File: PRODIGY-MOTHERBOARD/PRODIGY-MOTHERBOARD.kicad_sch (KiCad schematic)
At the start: 0 parts

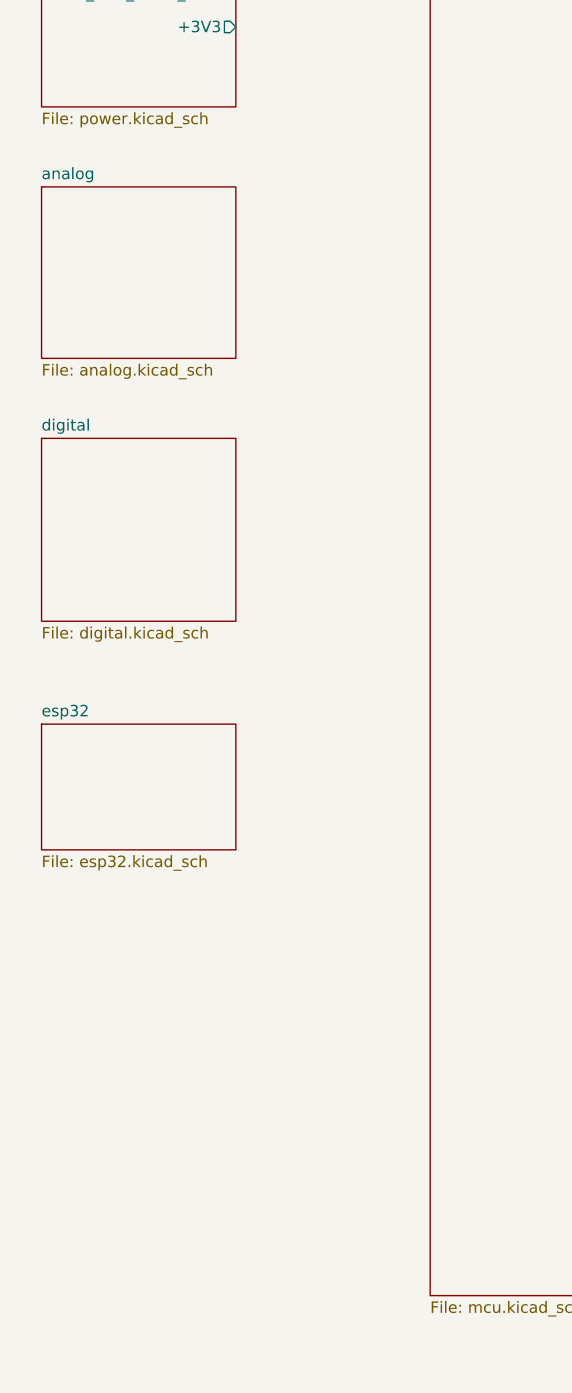
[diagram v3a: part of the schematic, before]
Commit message: Finished neopixel and button's schematic.
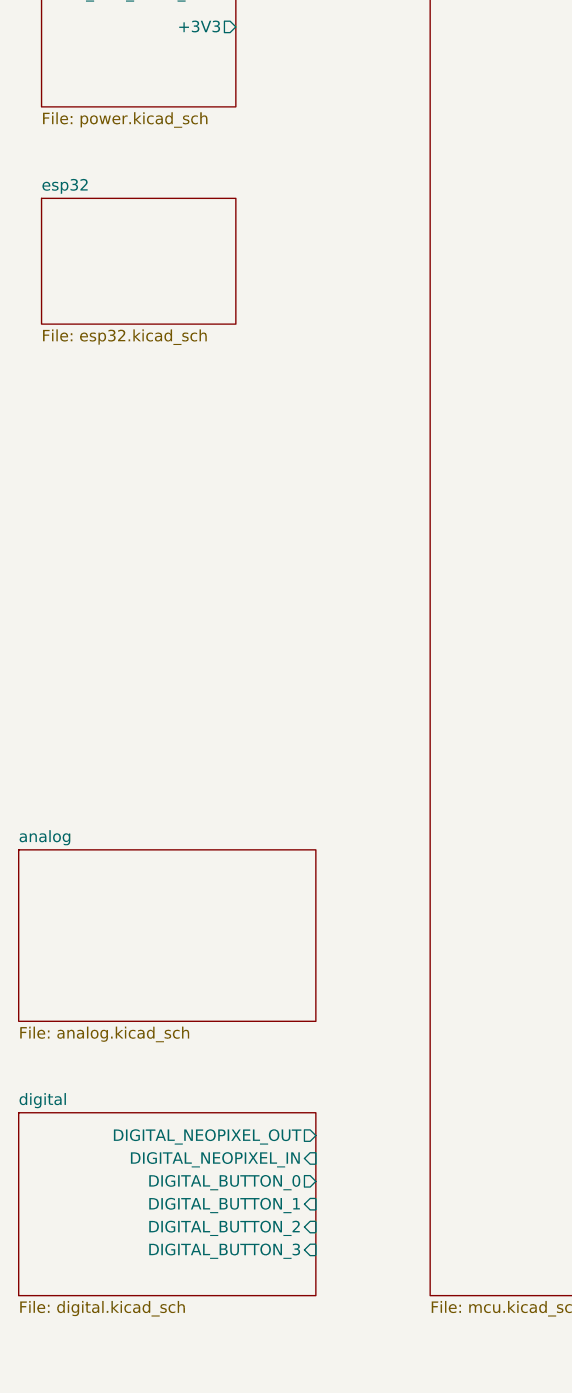
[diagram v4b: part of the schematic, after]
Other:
- sheet digital ports: added DIGITAL_BUTTON_0, DIGITAL_BUTTON_1, DIGITAL_BUTTON_2, DIGITAL_BUTTON_3, DIGITAL_NEOPIXEL_IN, DIGITAL_NEOPIXEL_OUT; removed none
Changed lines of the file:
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@@
 	)
 	(sheet
-		(at 39.37 114.3)
+		(at 39.37 55.88)
 		(size 21.59 13.97)
 		(fields_autoplaced yes)
@@
 		)
 		(property "Sheetname" "esp32"
-			(at 39.37 113.5884 0)
+			(at 39.37 55.1684 0)
 			(effects
 				(font
@@
 		)
 		(property "Sheetfile" "esp32.kicad_sch"
-			(at 39.37 128.8546 0)
+			(at 39.37 70.4346 0)
 			(effects
 				(font
@@
 		)
 		(property "Field2" ""
-			(at 39.37 114.3 0)
+			(at 39.37 55.88 0)
 			(effects
 				(font
@@
 	)
 	(sheet
-		(at 39.37 54.61)
-		(size 21.59 19.05)
+		(at 36.83 128.27)
+		(size 33.02 19.05)
 		(fields_autoplaced yes)
 		(stroke
@@
 		)
 		(property "Sheetname" "analog"
-			(at 39.37 53.8984 0)
+			(at 36.83 127.5584 0)
 			(effects
 				(font
@@
 		)
 		(property "Sheetfile" "analog.kicad_sch"
-			(at 39.37 74.2446 0)
+			(at 36.83 147.9046 0)
 			(effects
 				(font
@@
 		)
 		(property "Field2" ""
-			(at 39.37 54.61 0)
+			(at 36.83 128.27 0)
 			(effects
 				(font
@@
 	)
 	(sheet
-		(at 39.37 82.55)
-		(size 21.59 20.32)
+		(at 36.83 157.48)
+		(size 33.02 20.32)
 		(fields_autoplaced yes)
 		(stroke
@@
 		)
 		(property "Sheetname" "digital"
-			(at 39.37 81.8384 0)
+			(at 36.83 156.7684 0)
 			(effects
 				(font
@@
 		)
 		(property "Sheetfile" "digital.kicad_sch"
-			(at 39.37 103.4546 0)
+			(at 36.83 178.3846 0)
 			(effects
 				(font
@@
 			)
 		)
+		(pin "DIGITAL_NEOPIXEL_IN" input
+			(at 69.85 162.56 0)
+			(effects
+				(font
+					(size 1.27 1.27)
+				)
+				(justify right)
+			)
+		)
+		(pin "DIGITAL_NEOPIXEL_OUT" output
+			(at 69.85 160.02 0)
+			(effects
+				(font
+					(size 1.27 1.27)
+				)
+				(justify right)
+			)
+		)
+		(pin "DIGITAL_BUTTON_1" input
+			(at 69.85 167.64 0)
+			(effects
+				(font
+					(size 1.27 1.27)
+				)
+				(justify right)
+			)
+		)
+		(pin "DIGITAL_BUTTON_2" input
+			(at 69.85 170.18 0)
+			(effects
+				(font
+					(size 1.27 1.27)
+				)
+				(justify right)
+			)
+		)
+		(pin "DIGITAL_BUTTON_3" input
+			(at 69.85 172.72 0)
+			(effects
+				(font
+					(size 1.27 1.27)
+				)
+				(justify right)
+			)
+		)
+		(pin "DIGITAL_BUTTON_0" output
+			(at 69.85 165.1 0)
+			(effects
+				(font
+					(size 1.27 1.27)
+				)
+				(justify right)
+			)
+		)

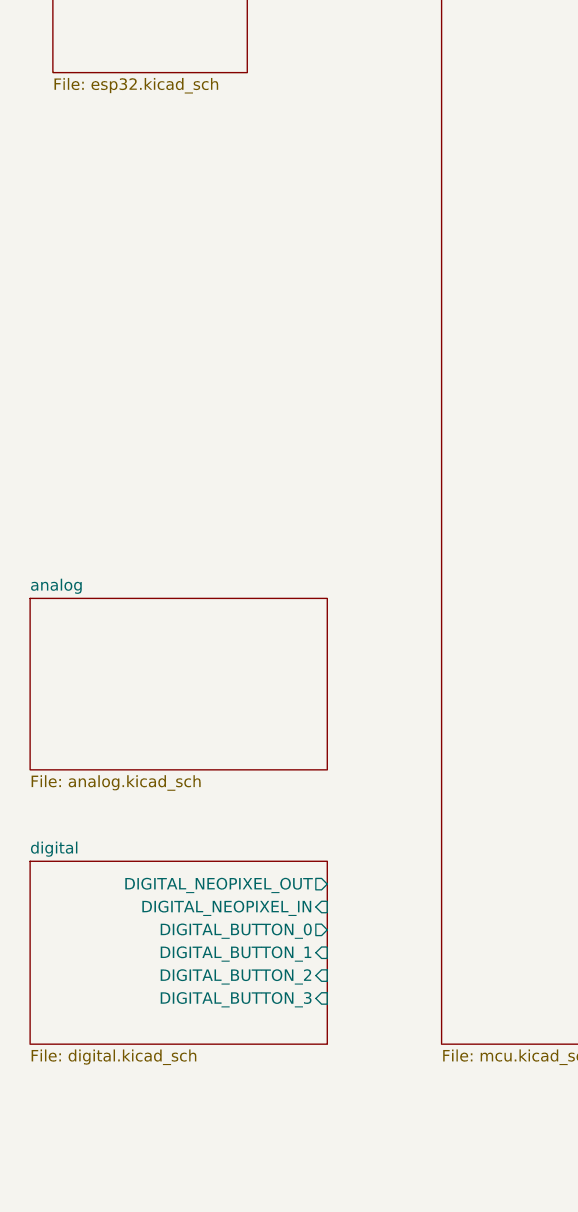
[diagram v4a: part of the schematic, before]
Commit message: LEDs schematic done.
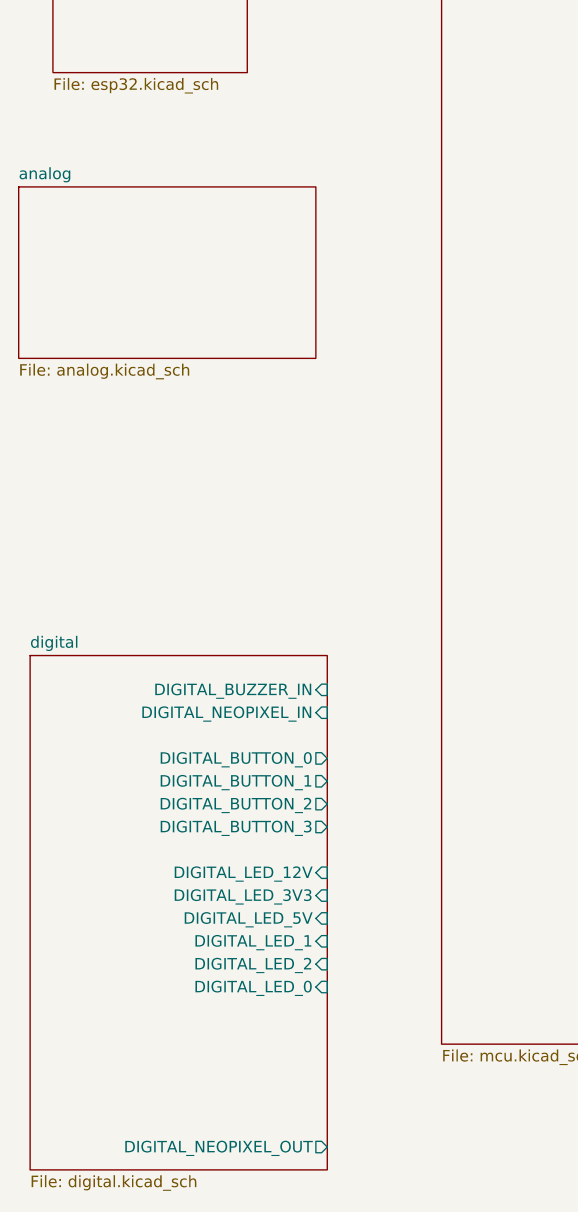
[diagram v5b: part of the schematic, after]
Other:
- sheet digital ports: added DIGITAL_BUZZER_IN, DIGITAL_LED_0, DIGITAL_LED_1, DIGITAL_LED_12V, DIGITAL_LED_2, DIGITAL_LED_3V3, DIGITAL_LED_5V; removed none
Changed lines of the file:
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@@
 	)
 	(sheet
-		(at 36.83 128.27)
+		(at 35.56 82.55)
 		(size 33.02 19.05)
 		(fields_autoplaced yes)
@@
 		)
 		(property "Sheetname" "analog"
-			(at 36.83 127.5584 0)
+			(at 35.56 81.8384 0)
 			(effects
 				(font
@@
 		)
 		(property "Sheetfile" "analog.kicad_sch"
-			(at 36.83 147.9046 0)
+			(at 35.56 102.1846 0)
 			(effects
 				(font
@@
 		)
 		(property "Field2" ""
-			(at 36.83 128.27 0)
+			(at 35.56 82.55 0)
 			(effects
 				(font
@@
 	)
 	(sheet
-		(at 36.83 157.48)
-		(size 33.02 20.32)
+		(at 36.83 134.62)
+		(size 33.02 57.15)
 		(fields_autoplaced yes)
 		(stroke
@@
 		)
 		(property "Sheetname" "digital"
-			(at 36.83 156.7684 0)
+			(at 36.83 133.9084 0)
 			(effects
 				(font
@@
 		)
 		(property "Sheetfile" "digital.kicad_sch"
-			(at 36.83 178.3846 0)
+			(at 36.83 192.3546 0)
 			(effects
 				(font
@@
 		)
 		(pin "DIGITAL_NEOPIXEL_IN" input
-			(at 69.85 162.56 0)
+			(at 69.85 140.97 0)
 			(effects
 				(font
@@
 		)
 		(pin "DIGITAL_NEOPIXEL_OUT" output
-			(at 69.85 160.02 0)
-			(effects
-				(font
-					(size 1.27 1.27)
-				)
-				(justify right)
-			)
-		)
-		(pin "DIGITAL_BUTTON_1" input
-			(at 69.85 167.64 0)
-			(effects
-				(font
-					(size 1.27 1.27)
-				)
-				(justify right)
-			)
-		)
-		(pin "DIGITAL_BUTTON_2" input
-			(at 69.85 170.18 0)
-			(effects
-				(font
-					(size 1.27 1.27)
-				)
-				(justify right)
-			)
-		)
-		(pin "DIGITAL_BUTTON_3" input
-			(at 69.85 172.72 0)
+			(at 69.85 189.23 0)
 			(effects
 				(font
@@
 		)
 		(pin "DIGITAL_BUTTON_0" output
-			(at 69.85 165.1 0)
-			(effects
-				(font
+			(at 69.85 146.05 0)
+			(effects
+				(font
+					(size 1.27 1.27)
+				)
+				(justify right)
+			)
+		)
+		(pin "DIGITAL_BUZZER_IN" input
+			(at 69.85 138.43 0)
+			(effects
+				(font
+					(size 1.27 1.27)
+				)
+				(justify right)
+			)
+		)
+		(pin "DIGITAL_BUTTON_1" output
+			(at 69.85 148.59 0)
+			(effects
+				(font
+					(size 1.27 1.27)
+				)
+				(justify right)
+			)
+		)
+		(pin "DIGITAL_BUTTON_3" output
+			(at 69.85 153.67 0)
+			(effects
+				(font
+					(size 1.27 1.27)
+				)
+				(justify right)
+			)
+		)
+		(pin "DIGITAL_BUTTON_2" output
+			(at 69.85 151.13 0)
+			(effects
+				(font
+					(size 1.27 1.27)
+				)
+				(justify right)
+			)
+		)
+		(pin "DIGITAL_LED_12V" input
+			(at 69.85 158.75 0)
+			(effects
+				(font
+					(size 1.27 1.27)
+				)
+				(justify right)
+			)
+		)
+		(pin "DIGITAL_LED_3V3" input
+			(at 69.85 161.29 0)
+			(effects
+				(font
+					(size 1.27 1.27)
+				)
+				(justify right)
+			)
+		)
+		(pin "DIGITAL_LED_5V" input
+			(at 69.85 163.83 0)
+			(effects
+				(font
+					(size 1.27 1.27)
+				)
+				(justify right)
+			)
+		)
+		(pin "DIGITAL_LED_1" input
+			(at 69.85 166.37 0)
+			(effects
+				(font
+					(size 1.27 1.27)
+				)
+				(justify right)
+			)
+		)
+		(pin "DIGITAL_LED_2" input
+			(at 69.85 168.91 0)
+			(effects
+				(font
+					(size 1.27 1.27)
+				)
+				(justify right)
+			)
+		)
+		(pin "DIGITAL_LED_0" input
+			(at 69.85 171.45 0)
+			(effects
+				(font

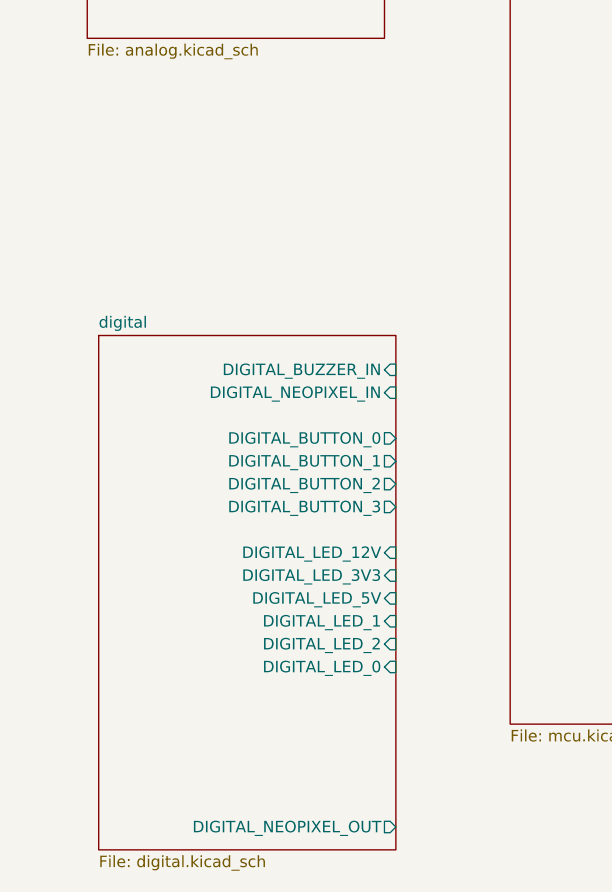
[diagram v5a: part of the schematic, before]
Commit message: Digital section done.
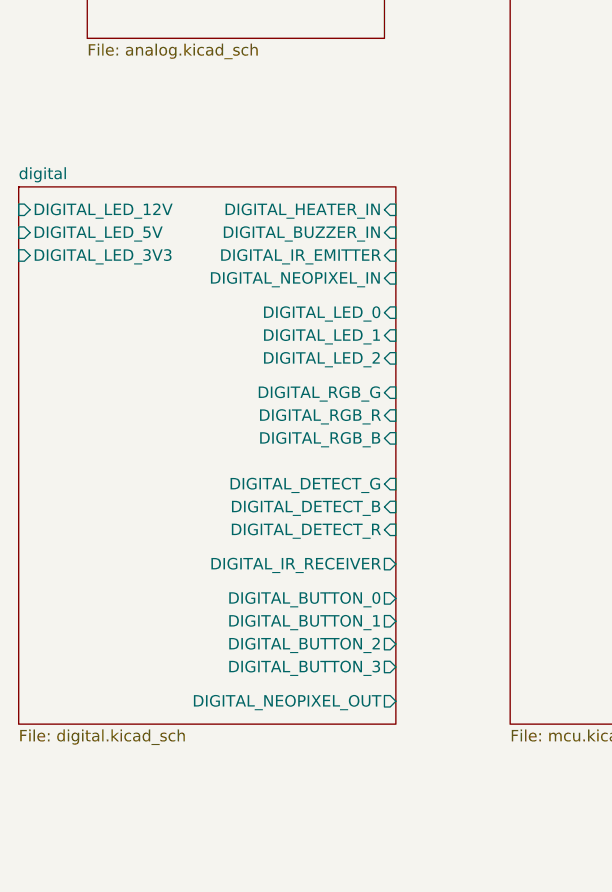
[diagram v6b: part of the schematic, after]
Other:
- sheet digital ports: added DIGITAL_DETECT_B, DIGITAL_DETECT_G, DIGITAL_DETECT_R, DIGITAL_HEATER_IN, DIGITAL_IR_EMITTER, DIGITAL_IR_RECEIVER, DIGITAL_RGB_B, DIGITAL_RGB_G, DIGITAL_RGB_R; removed none
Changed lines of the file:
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@@
 	)
 	(sheet
-		(at 36.83 134.62)
-		(size 33.02 57.15)
+		(at 27.94 118.11)
+		(size 41.91 59.69)
 		(fields_autoplaced yes)
 		(stroke
@@
 		)
 		(property "Sheetname" "digital"
-			(at 36.83 133.9084 0)
+			(at 27.94 117.3984 0)
 			(effects
 				(font
@@
 		)
 		(property "Sheetfile" "digital.kicad_sch"
-			(at 36.83 192.3546 0)
+			(at 27.94 178.3846 0)
 			(effects
 				(font
@@
 		)
 		(pin "DIGITAL_NEOPIXEL_IN" input
+			(at 69.85 128.27 0)
+			(effects
+				(font
+					(size 1.27 1.27)
+				)
+				(justify right)
+			)
+		)
+		(pin "DIGITAL_NEOPIXEL_OUT" output
+			(at 69.85 175.26 0)
+			(effects
+				(font
+					(size 1.27 1.27)
+				)
+				(justify right)
+			)
+		)
+		(pin "DIGITAL_BUTTON_0" output
+			(at 69.85 163.83 0)
+			(effects
+				(font
+					(size 1.27 1.27)
+				)
+				(justify right)
+			)
+		)
+		(pin "DIGITAL_BUZZER_IN" input
+			(at 69.85 123.19 0)
+			(effects
+				(font
+					(size 1.27 1.27)
+				)
+				(justify right)
+			)
+		)
+		(pin "DIGITAL_BUTTON_1" output
+			(at 69.85 166.37 0)
+			(effects
+				(font
+					(size 1.27 1.27)
+				)
+				(justify right)
+			)
+		)
+		(pin "DIGITAL_BUTTON_3" output
+			(at 69.85 171.45 0)
+			(effects
+				(font
+					(size 1.27 1.27)
+				)
+				(justify right)
+			)
+		)
+		(pin "DIGITAL_BUTTON_2" output
+			(at 69.85 168.91 0)
+			(effects
+				(font
+					(size 1.27 1.27)
+				)
+				(justify right)
+			)
+		)
+		(pin "DIGITAL_LED_12V" input
+			(at 27.94 120.65 180)
+			(effects
+				(font
+					(size 1.27 1.27)
+				)
+				(justify left)
+			)
+		)
+		(pin "DIGITAL_LED_3V3" input
+			(at 27.94 125.73 180)
+			(effects
+				(font
+					(size 1.27 1.27)
+				)
+				(justify left)
+			)
+		)
+		(pin "DIGITAL_LED_5V" input
+			(at 27.94 123.19 180)
+			(effects
+				(font
+					(size 1.27 1.27)
+				)
+				(justify left)
+			)
+		)
+		(pin "DIGITAL_LED_1" input
+			(at 69.85 134.62 0)
+			(effects
+				(font
+					(size 1.27 1.27)
+				)
+				(justify right)
+			)
+		)
+		(pin "DIGITAL_LED_2" input
+			(at 69.85 137.16 0)
+			(effects
+				(font
+					(size 1.27 1.27)
+				)
+				(justify right)
+			)
+		)
+		(pin "DIGITAL_LED_0" input
+			(at 69.85 132.08 0)
+			(effects
+				(font
+					(size 1.27 1.27)
+				)
+				(justify right)
+			)
+		)
+		(pin "DIGITAL_RGB_G" input
 			(at 69.85 140.97 0)
 			(effects
@@
 			)
 		)
-		(pin "DIGITAL_NEOPIXEL_OUT" output
-			(at 69.85 189.23 0)
-			(effects
-				(font
-					(size 1.27 1.27)
-				)
-				(justify right)
-			)
-		)
-		(pin "DIGITAL_BUTTON_0" output
+		(pin "DIGITAL_RGB_R" input
+			(at 69.85 143.51 0)
+			(effects
+				(font
+					(size 1.27 1.27)
+				)
+				(justify right)
+			)
+		)
+		(pin "DIGITAL_RGB_B" input
 			(at 69.85 146.05 0)
 			(effects
@@
 			)
 		)
-		(pin "DIGITAL_BUZZER_IN" input
-			(at 69.85 138.43 0)
-			(effects
-				(font
-					(size 1.27 1.27)
-				)
-				(justify right)
-			)
-		)
-		(pin "DIGITAL_BUTTON_1" output
-			(at 69.85 148.59 0)
-			(effects
-				(font
-					(size 1.27 1.27)
-				)
-				(justify right)
-			)
-		)
-		(pin "DIGITAL_BUTTON_3" output
+		(pin "DIGITAL_DETECT_G" input
+			(at 69.85 151.13 0)
+			(effects
+				(font
+					(size 1.27 1.27)
+				)
+				(justify right)
+			)
+		)
+		(pin "DIGITAL_DETECT_B" input
 			(at 69.85 153.67 0)
 			(effects
@@
 			)
 		)
-		(pin "DIGITAL_BUTTON_2" output
-			(at 69.85 151.13 0)
-			(effects
-				(font
-					(size 1.27 1.27)
-				)
-				(justify right)
-			)
-		)
-		(pin "DIGITAL_LED_12V" input
-			(at 69.85 158.75 0)
-			(effects
-				(font
-					(size 1.27 1.27)
-				)
-				(justify right)
-			)
-		)
-		(pin "DIGITAL_LED_3V3" input
-			(at 69.85 161.29 0)
-			(effects
-				(font
-					(size 1.27 1.27)
-				)
-				(justify right)
-			)
-		)
-		(pin "DIGITAL_LED_5V" input
-			(at 69.85 163.83 0)
-			(effects
-				(font
-					(size 1.27 1.27)
-				)
-				(justify right)
-			)
-		)
-		(pin "DIGITAL_LED_1" input
-			(at 69.85 166.37 0)
-			(effects
-				(font
-					(size 1.27 1.27)
-				)
-				(justify right)
-			)
-		)
-		(pin "DIGITAL_LED_2" input
-			(at 69.85 168.91 0)
-			(effects
-				(font
-					(size 1.27 1.27)
-				)
-				(justify right)
-			)
-		)
-		(pin "DIGITAL_LED_0" input
-			(at 69.85 171.45 0)
-			(effects
-				(font
+		(pin "DIGITAL_DETECT_R" input
+			(at 69.85 156.21 0)
+			(effects
+				(font
+					(size 1.27 1.27)
+				)
+				(justify right)
+			)
+		)
+		(pin "DIGITAL_IR_EMITTER" input
+			(at 69.85 125.73 0)
+			(effects
+				(font
+					(size 1.27 1.27)
+				)
+				(justify right)
+			)
+		)
+		(pin "DIGITAL_IR_RECEIVER" output
+			(at 69.85 160.02 0)
+			(effects
+				(font
+					(size 1.27 1.27)
+				)
+				(justify right)
+			)
+		)
+		(pin "DIGITAL_HEATER_IN" input
+			(at 69.85 120.65 0)
+			(effects
+				(font

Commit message: CAN schematic done
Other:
- sheet CAN ports: added CAN_EN, CAN_H, CAN_L, CAN_RX, CAN_SILENT, CAN_TX; removed none
- sheet MOTOR ports: added MOTOR_IN1_1, MOTOR_IN1_2, MOTOR_IN2_1, MOTOR_IN2_2, MOTOR_OUT1_BREAKOUT_1, MOTOR_OUT1_BREAKOUT_2, MOTOR_OUT2_BREAKOUT_1, MOTOR_OUT2_BREAKOUT_2; removed none
- sheet OUTPUTS ports: added BREAKOUT_CAN_H, BREAKOUT_CAN_L; removed BREAKOUT_CAN_RX, BREAKOUT_CAN_TX, BREAKOUT_SERVO_0, BREAKOUT_SERVO_1, BREAKOUT_SERVO_2, BREAKOUT_ULTRASONIC_ECHO, BREAKOUT_ULTRASONIC_TRIG
- note added: "59/64 pins"
- note removed: "57/64 pins"
